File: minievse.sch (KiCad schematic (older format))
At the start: 42 parts, among them IC1 ATMEGA328P-P, K1 RELAY, K2 RELAY, P1 SERIAL, P2 5V input, P3 ICSP, P4 Pilot, P5 RELAY120V, P6 RELAY240V, P7 RELAY_CTRL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

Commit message: replace relays with triacs, update schematic
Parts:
- removed D1, D2: D_Schottky, symbol D_Schottky
- removed K1, K2: RELAY, symbol RELAY_2RT
- removed P5: RELAY120V, battery-dlg:CCFLHV, symbol CONN_01X02
- removed P6: RELAY240V, battery-dlg:CCFLHV, symbol CONN_01X02
- removed Q1, Q2: 2N7000, symbol FET_N
- added U2, U3: MOC3021M, DIP-6, symbol MOC3021M
- R1, R8: value 10K -> 270
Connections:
- net labels removed: VDD
- wire segments 69 -> 61
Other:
- note added: "R4 RATED SAME AS\n120V RELAY COIL"
- note added: "THESE TRIACS CLOSE WHEN 120VAC OR 240VAC IS READY"
- note added: "THIS CONNECTOR TO BIG 50A RELAY WITH 120V COIL"
- note removed: "THIS CONNECTOR ACTIVATES GIANT 50A RELAY WITH 120V COIL"
- note removed: "THIS RELAY CLOSES WHEN 120VAC IS READY"
- note removed: "THIS RELAY CLOSES WHEN 240VAC IS READY"
- moved on the sheet: P7, R1, R4, R5, R6, R7

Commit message: fix U1 wiring, choose a part for D3
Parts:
- removed R11, R9: 2700, Resistors_ThroughHole:Resistor_Horizontal_RM10mm, symbol R
- C10, C7, C8, C9: footprint (none) -> Capacitors_ThroughHole:C_Radial_D5_L6_P2.5
- D3: value 13V TVS -> P6KE16CA; footprint (none) -> DO-15
- R12, R13: value 2700 -> 1200
- U2, U3: footprint DIP-6 -> (none)
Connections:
- wire segments 61 -> 58

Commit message: inductor control of big relay
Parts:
- added L1, L2: INDUCTOR, symbol INDUCTOR
- added U4: MOC3021M, symbol MOC3021M
- R4: value 100 -> 270
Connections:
- net labels added: RELAY_SOFT
- wire segments 58 -> 72
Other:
- note added: "THESE TRIACS CONTROL RELAY COIL CURRENT"
- note removed: "R4 RATED SAME AS\n120V RELAY COIL"
- note removed: "THESE TRIACS CLOSE WHEN 120VAC OR 240VAC IS READY"
- moved on the sheet: P7, R1, R8, U2, U3

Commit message: sense AC voltage, dim relay coil, LED strip, amp knob
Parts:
- removed L1, L2: INDUCTOR, symbol INDUCTOR
- removed U3, U4: MOC3021M, symbol MOC3021M
- added C11, C12, C13, C14: 10uF, symbol CAPAPOL
- added C15: C, symbol C
- added D1, D2: 1N4007, symbol D
- added P5: AC_GND_AC, symbol CONN_01X03
- added P6: LED_STRIP, symbol CONN_01X03
- added R11, R9: 2550, symbol R
- added R14, R15: 50K, symbol R
- added R16, R17: 30K, symbol R
- added R18: 10K, symbol R
- added R19: R, symbol R
- added RV1: POT, symbol POT
- added U3: LTV-354T, MFSOP-6, symbol LTV-354T
- P7: value RELAY_CTRL -> RELAY_COIL
- R1: value 270 -> 220
- R4, R8: value 270 -> 2550
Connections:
- net labels added: AC_SENSE_1, AC_SENSE_2, AC_ZEROX, AMP_KNOB, LED_DATA, RELAY_TRIAC
- net labels removed: AMP_READ, RELAY_120V, RELAY_240V, RELAY_SOFT
- wire segments 72 -> 73
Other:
- note added: "a word on triacs controlling inductive loads:\nhttp://www.instructables.com/id/Arduino-controlled-light-dimmer-The-circuit/step2/A-word-on-inductive-loads-theory/"
- note added: "coil snubber"
- note removed: "THESE TRIACS CONTROL RELAY COIL CURRENT"
- moved on the sheet: P7, R1, U2

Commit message: replace zero crossing opto, assign footprints
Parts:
- removed U3: LTV-354T, MFSOP-6, symbol LTV-354T
- added U3: H11AA, Housings_DIP:DIP-6_W7.62mm_LongPads, symbol H11AA
- C11, C12, C13, C14: footprint (none) -> Capacitors_ThroughHole:C_Radial_D5_L6_P2.5
- D1, D2: footprint (none) -> Diodes_ThroughHole:Diode_DO-41_SOD81_Horizontal_RM10
- D3: footprint DO-15 -> Diodes_ThroughHole:Diode_DO-41_SOD81_Horizontal_RM10
- P5: footprint (none) -> Connect:bornier3
- P6: footprint (none) -> Connect:PINHEAD1-3
- R1, R11, R14, R15, R18, R4, R8, R9: footprint (none) -> Resistors_ThroughHole:Resistor_Horizontal_RM10mm
- R16, R17: value 30K -> 15K; footprint (none) -> Resistors_ThroughHole:Resistor_Horizontal_RM10mm
- RV1: footprint (none) -> Potentiometers:Potentiometer_Triwood_RM-065
- U1: footprint (none) -> Housings_DIP:DIP-16_W7.62mm_LongPads
- U2: footprint (none) -> Housings_DIP:DIP-6_W7.62mm_LongPads
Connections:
- wire segments 73 -> 75

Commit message: c10 polarized cap was backwards
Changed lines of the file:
@@
 F 3 "" H 8500 2350 300 0000 C CNN
 	1    8500 2350
-	-1   0    0    1
+	1    0    0    -1
 $EndComp
 $Comp
@@
 L GND #PWR030
 U 1 1 5726BDA4
-P 6250 6050
-F 0 "#PWR030" H 6250 5800 50  0001 C CNN
-F 1 "GND" H 6250 5900 50  0000 C CNN
-F 2 "" H 6250 6050 50  0000 C CNN
-F 3 "" H 6250 6050 50  0000 C CNN
-	1    6250 6050
-	1    0    0    -1
+P 6250 5850
+F 0 "#PWR030" H 6250 5600 50  0001 C CNN
+F 1 "GND" H 6250 5700 50  0000 C CNN
+F 2 "" H 6250 5850 50  0000 C CNN
+F 3 "" H 6250 5850 50  0000 C CNN
+	1    6250 5850
+	-1   0    0    1
 $EndComp
 Text Label 6250 5500 2    60   ~ 0
@@
 F 3 "" H 5980 5950 50  0000 L CNN
 	1    5950 5950
-	1    0    0    -1
-$EndComp
-Wire Wire Line
+	1    0    0    1
+$EndComp
+Wire Wire Line

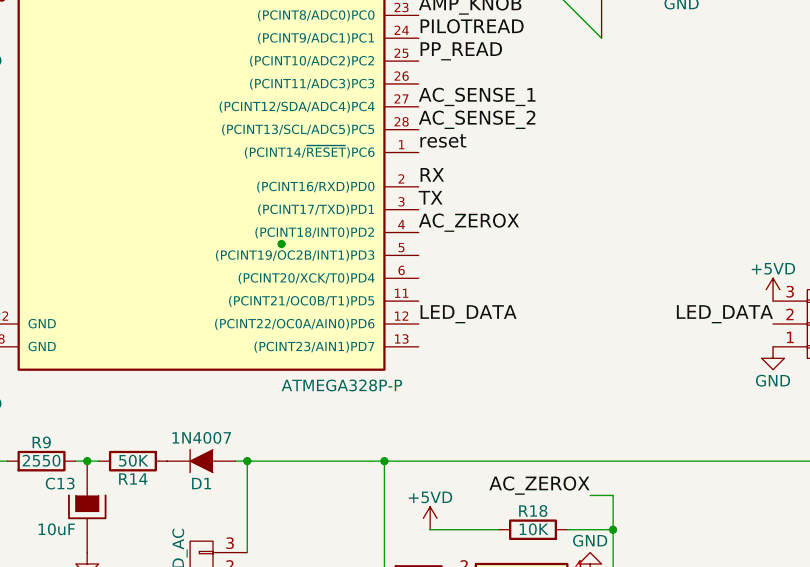
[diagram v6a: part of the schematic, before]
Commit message: change LED pin from 12 to 6 for wiring convenience
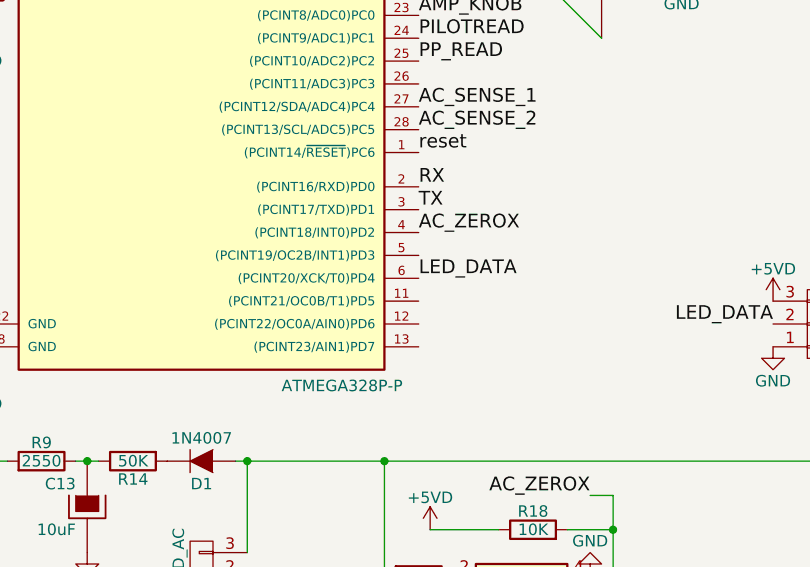
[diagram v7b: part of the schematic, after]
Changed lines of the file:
@@
 	4850 5850 4750 5850
 Connection ~ 3600 4850
-Connection ~ 4900 4400
 Connection ~ 3200 2550
 $Comp
@@
 Text Label 7050 4750 2    60   ~ 0
 LED_DATA
-Text Label 5500 4750 0    60   ~ 0
+Text Label 5500 4550 0    60   ~ 0
 LED_DATA
 $Comp

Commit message: rm max232, use bipolar +-12v supply and op-amp
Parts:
- removed C10, C7: 1uF, Capacitors_ThroughHole:C_Radial_D5_L6_P2.5, symbol CAPAPOL
- removed U1: MAX232, Housings_DIP:DIP-16_W7.62mm_LongPads, symbol MAX232
- added C7: C, symbol C
- added D4, D5: DIODESCH, symbol DIODESCH
- added L1, L2: INDUCTOR, symbol INDUCTOR
- added Q1: FET_N, symbol FET_N
- added Q2: FET_P, symbol FET_N
- added R20, R21: 1220, symbol R
- added R22: 22, symbol R
- added U1: LM7332, symbol LM7332
- C8, C9: value 1uF -> CAPAPOL; footprint Capacitors_ThroughHole:C_Radial_D5_L6_P2.5 -> (none)
- R12, R13: value 1200 -> 10K; footprint Resistors_ThroughHole:Resistor_Horizontal_RM10mm -> (none)
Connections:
- net labels added: +12VA, +2.5V, -12VA, BOOST12, BOOST5
